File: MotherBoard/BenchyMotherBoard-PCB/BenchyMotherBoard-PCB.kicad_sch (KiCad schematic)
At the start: 0 parts

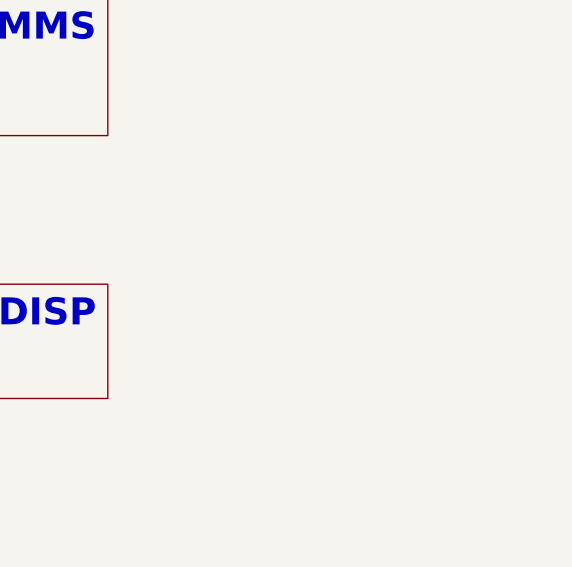
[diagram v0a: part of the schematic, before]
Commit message: (WIP) Added PS supervisor
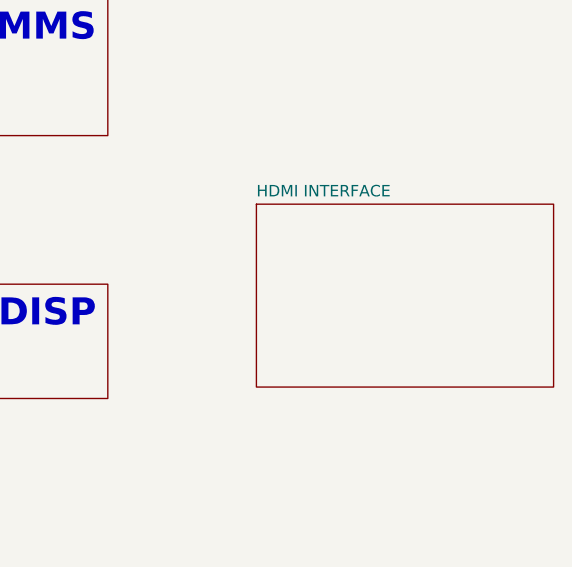
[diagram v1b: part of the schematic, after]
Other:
- added sheet HDMI INTERFACE (HDMI.kicad_sch)
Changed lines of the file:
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@@
   (title_block
     (title "Benchy Reloaded")
-    (rev "REV2")
+    (rev "REV3")
     (company "Daxxn Industries")
   )
@@
     )
     (instances
+      (project "BenchyMotherBoard-PCB"
+        (path "/2ea077fe-b0e6-467f-a1c1-8336ebdb7a86" (page "7"))
+      )
+    )
+  )
+  (sheet (at 257.81 54.61) (size 33.02 20.32) (fields_autoplaced)
+    (stroke (width 0.1524) (type solid))
+    (fill (color 0 0 0 0.0000))
+    (property "Sheetname" "HDMI INTERFACE" (at 257.81 53.8984 0)
+      (effects (font (size 1.27 1.27)) (justify left bottom))
+    )
+    (property "Sheetfile" "HDMI.kicad_sch" (at 257.81 75.5146 0)
+      (effects (font (size 1.27 1.27)) (justify left top) hide)
+    )
+    (instances
